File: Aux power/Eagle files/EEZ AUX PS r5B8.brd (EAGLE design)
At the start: 107 x 74 mm, 80 parts, among them IC16 LM25575, IC17 MC7812, IC18 TPD4E002DRLR, IC19 TPD2E001DZDR, IC20 ADUM3160BRWZ, Q20 BTA26-600, Q21 BTA26-600, Q22 IRLL014N, X10 826629-5, X11 2411-01, X4 282836-5, X5 09185067324, X6 22-23-2031, X7 LMJ2138812S0LOT6C, X8 826629-8, X9 826629-5

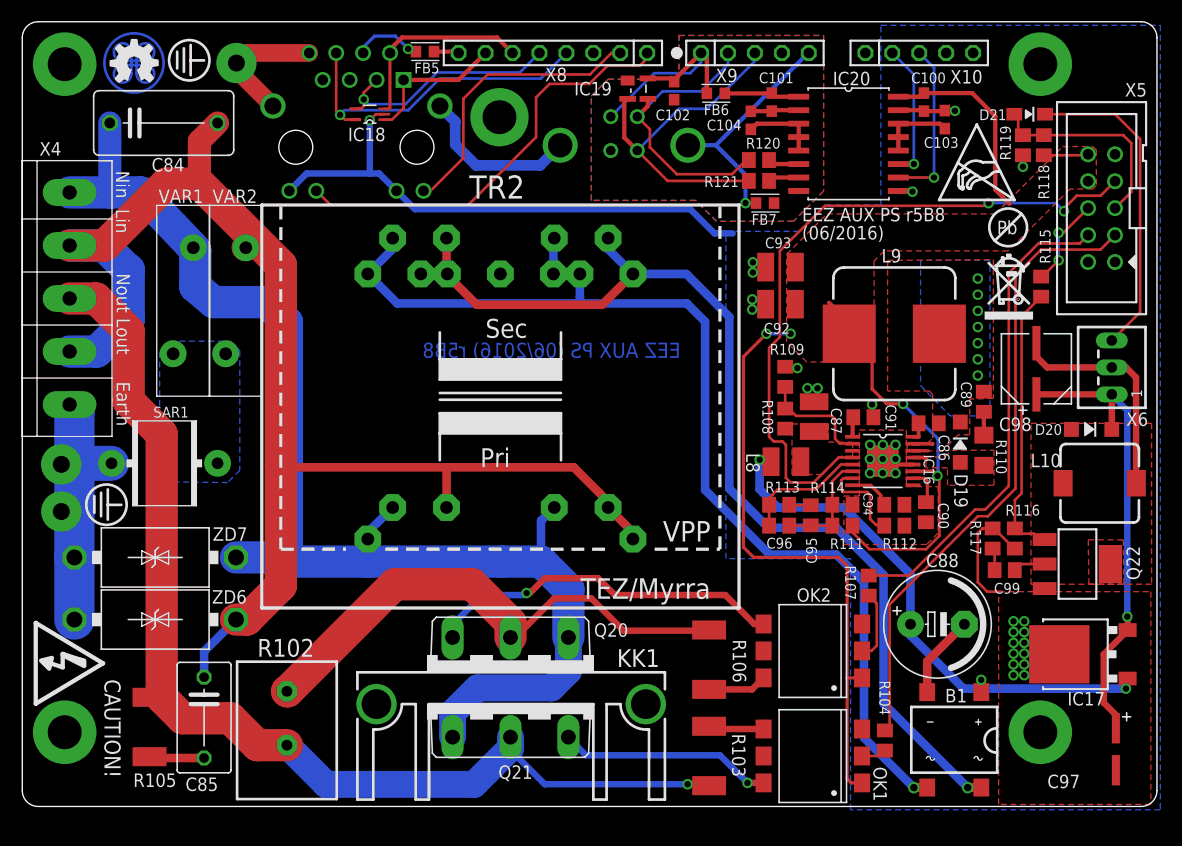
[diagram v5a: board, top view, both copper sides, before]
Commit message: PCB fiducials, outlines, milling bridges
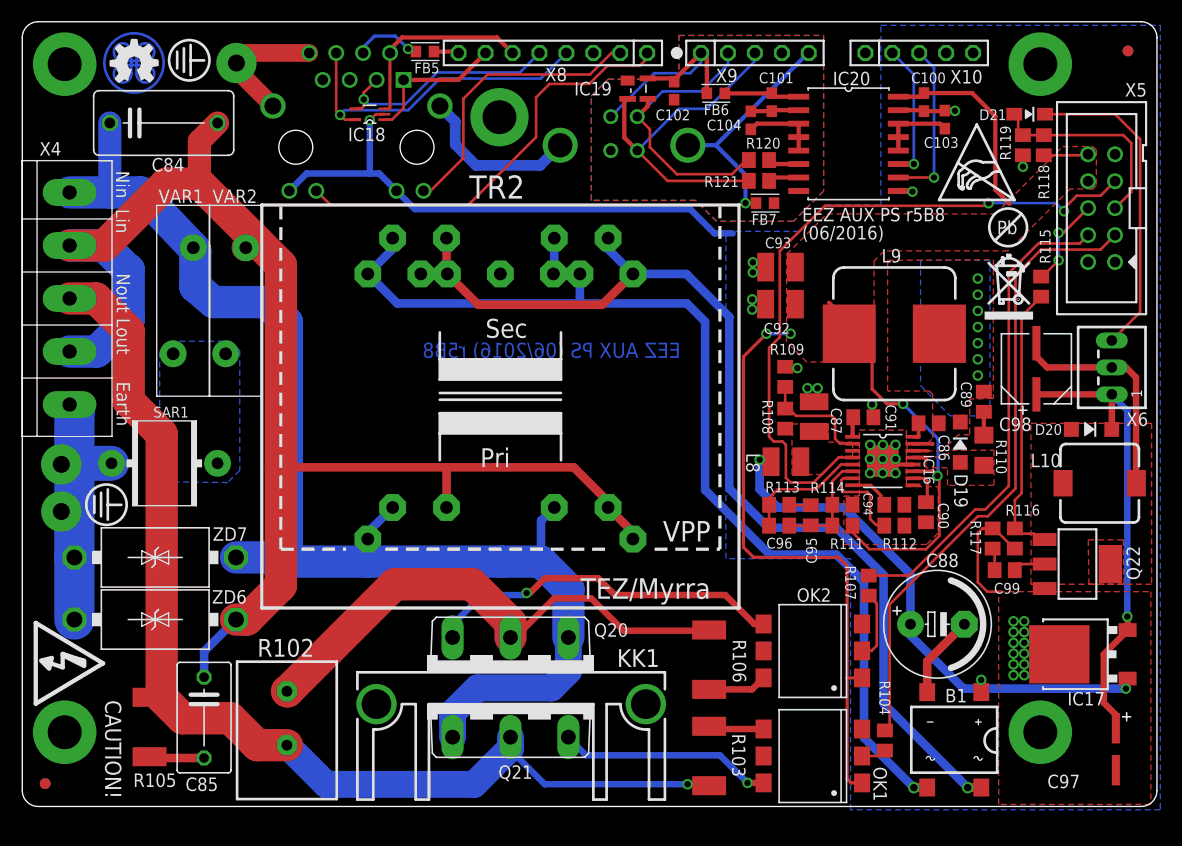
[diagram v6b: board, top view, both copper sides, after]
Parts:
- added U$13, U$14: FIDUCIAL_2, EEZ_Lib1:FIDUCIAL_DUAL
- TR2: value TEZ6/D230/12V -> TEZ6/D230/15V
